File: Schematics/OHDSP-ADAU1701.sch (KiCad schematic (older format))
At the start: 0 parts

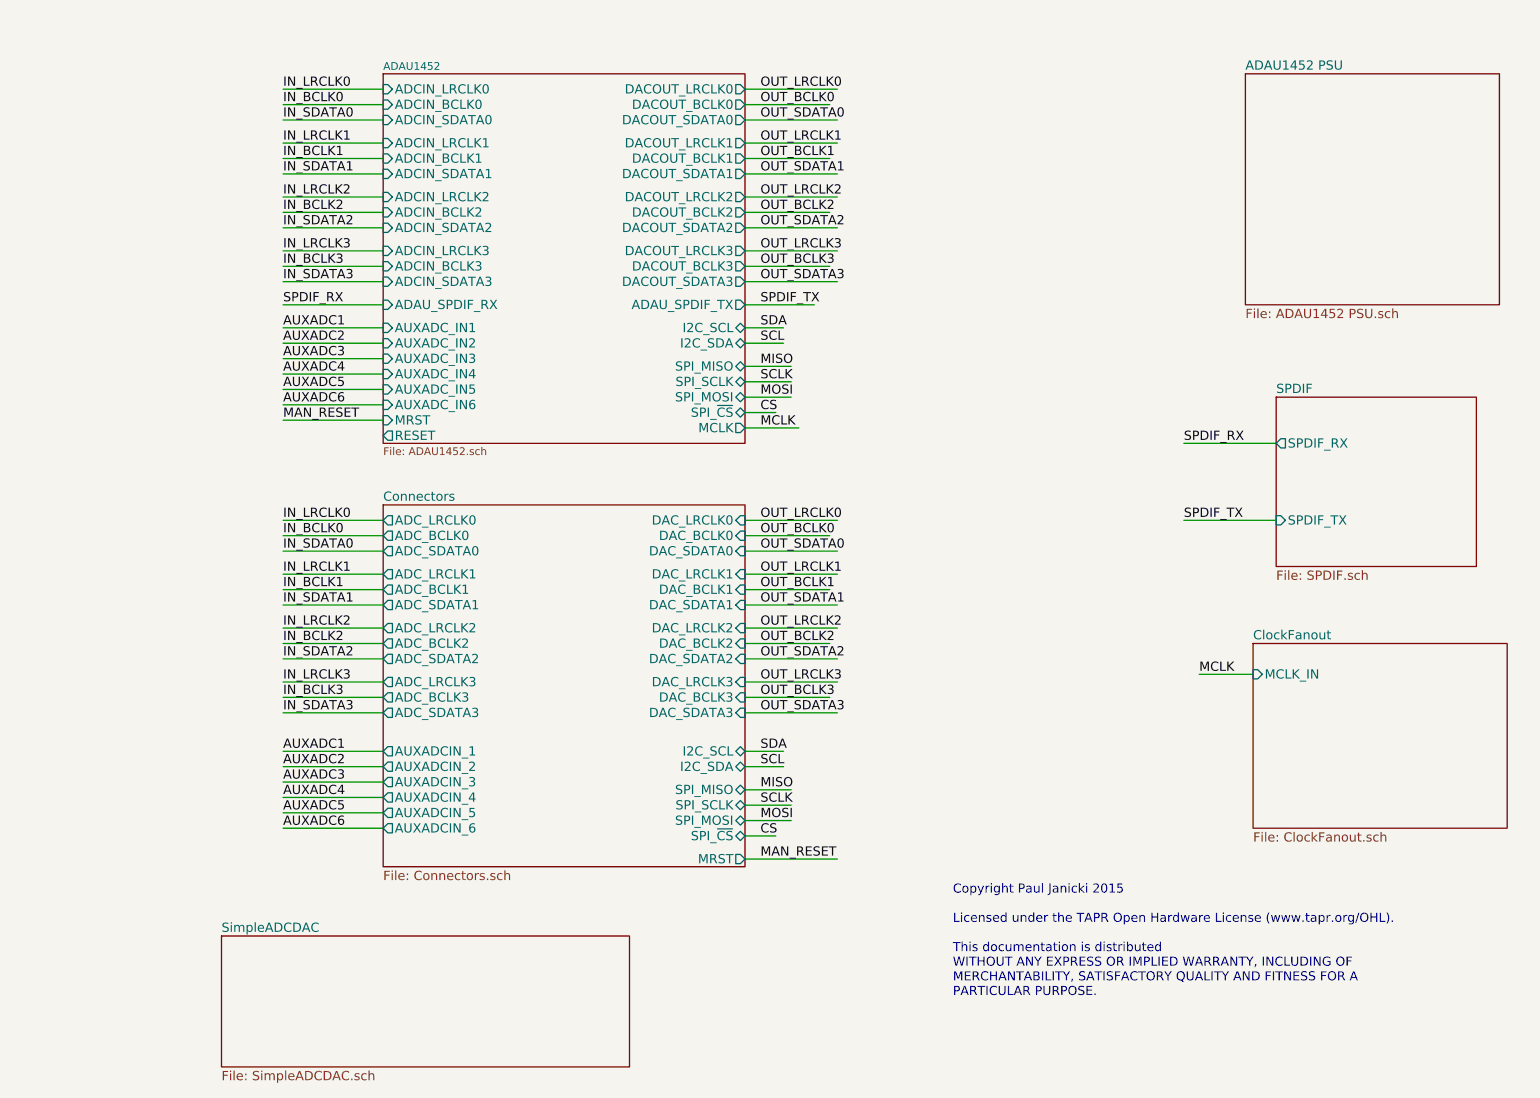
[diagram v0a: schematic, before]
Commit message: Adding ADAU1701 version
Because its easier...
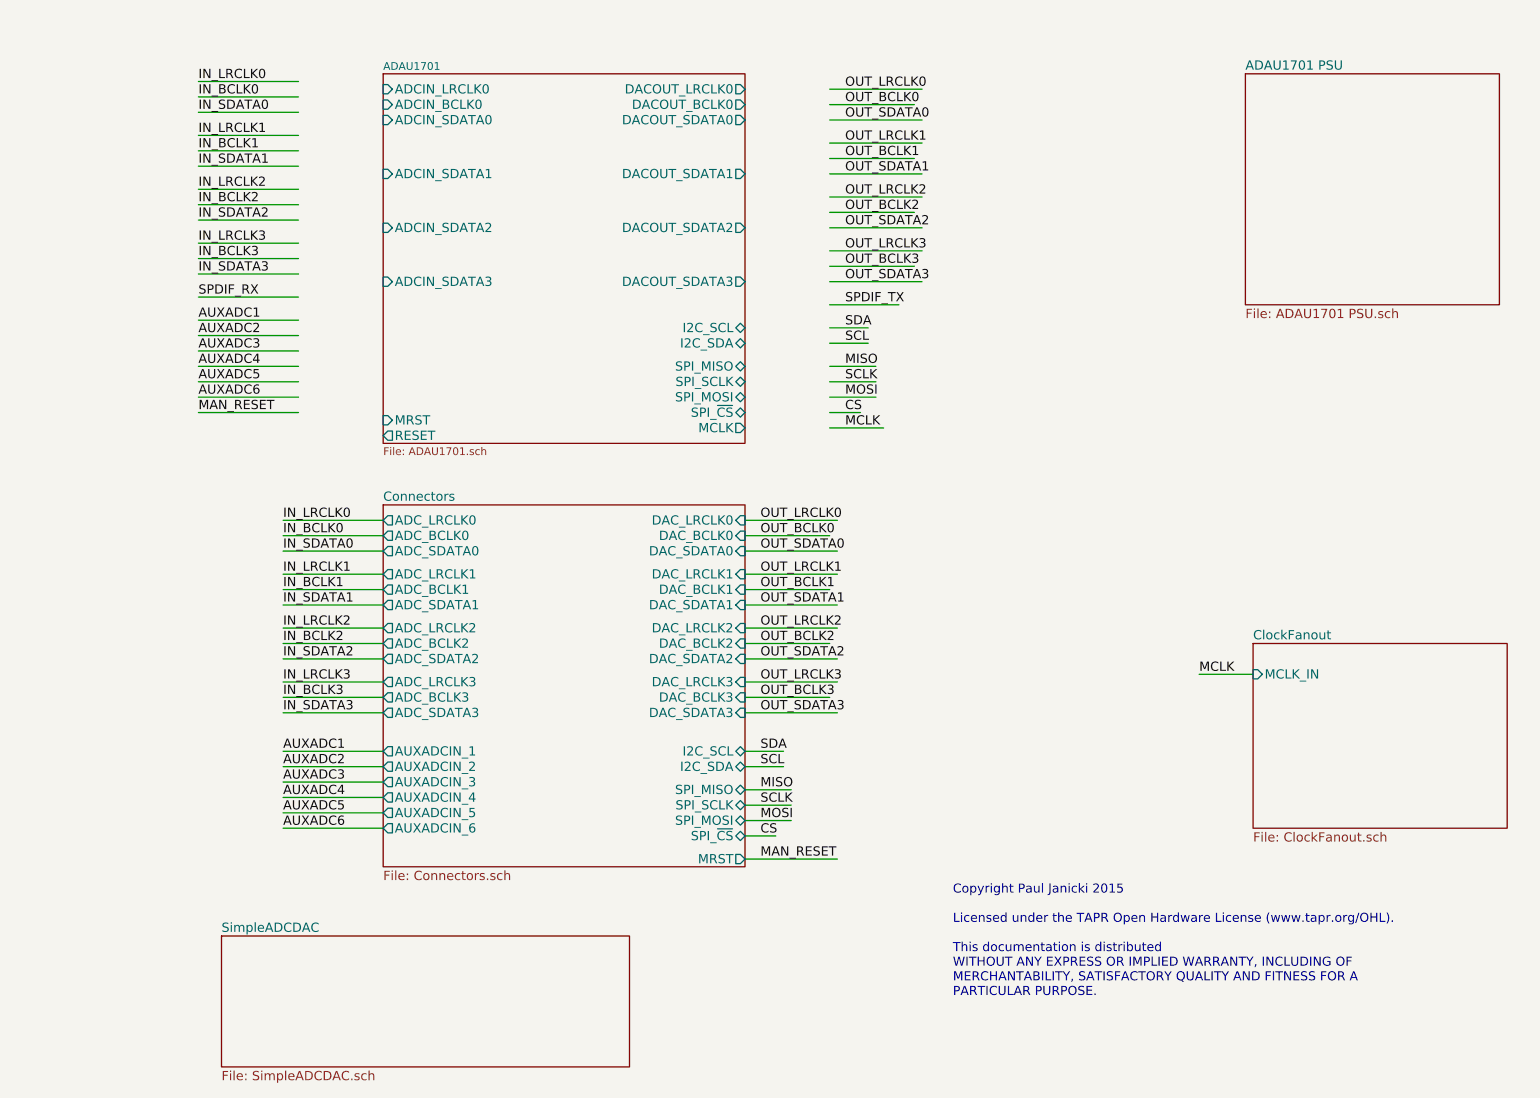
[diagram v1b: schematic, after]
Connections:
- wire segments 80 -> 78
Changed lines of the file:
@@
 LIBS:power
 LIBS:OHDSP-Lib
-LIBS:OHDSP-ADAU1452-cache
 EELAYER 25 0
 EELAYER END
 $Descr A4 11693 8268
 encoding utf-8
-Sheet 1 7
+Sheet 1 6
 Title ""
 Date "10 feb 2015"
@@
 S 3300 1100 2350 2400
 U 54BE4270
-F0 "ADAU1452" 50
-F1 "ADAU1452.sch" 50
+F0 "ADAU1701" 50
+F1 "ADAU1701.sch" 50
 F2 "ADCIN_LRCLK0" I L 3300 1200 60
 F3 "ADCIN_BCLK0" I L 3300 1300 60
 F4 "ADCIN_SDATA0" I L 3300 1400 60
-F5 "ADCIN_LRCLK1" I L 3300 1550 60
-F6 "ADCIN_BCLK1" I L 3300 1650 60
 F7 "ADCIN_SDATA1" I L 3300 1750 60
-F8 "ADCIN_LRCLK2" I L 3300 1900 60
-F9 "ADCIN_BCLK2" I L 3300 2000 60
 F10 "ADCIN_SDATA2" I L 3300 2100 60
-F11 "ADCIN_LRCLK3" I L 3300 2250 60
-F12 "ADCIN_BCLK3" I L 3300 2350 60
 F13 "ADCIN_SDATA3" I L 3300 2450 60
 F14 "DACOUT_LRCLK0" O R 5650 1200 60
 F15 "DACOUT_BCLK0" O R 5650 1300 60
 F16 "DACOUT_SDATA0" O R 5650 1400 60
-F17 "ADAU_SPDIF_RX" I L 3300 2600 60
-F18 "ADAU_SPDIF_TX" O R 5650 2600 60
-F19 "DACOUT_LRCLK1" O R 5650 1550 60
-F20 "DACOUT_BCLK1" O R 5650 1650 60
 F21 "DACOUT_SDATA1" O R 5650 1750 60
-F22 "DACOUT_LRCLK2" O R 5650 1900 60
-F23 "DACOUT_BCLK2" O R 5650 2000 60
 F24 "DACOUT_SDATA2" O R 5650 2100 60
-F25 "DACOUT_LRCLK3" O R 5650 2250 60
-F26 "DACOUT_BCLK3" O R 5650 2350 60
 F27 "DACOUT_SDATA3" O R 5650 2450 60
-F28 "AUXADC_IN1" I L 3300 2750 60
-F29 "AUXADC_IN2" I L 3300 2850 60
-F30 "AUXADC_IN3" I L 3300 2950 60
-F31 "AUXADC_IN4" I L 3300 3050 60
-F32 "AUXADC_IN5" I L 3300 3150 60
-F33 "AUXADC_IN6" I L 3300 3250 60
 F34 "I2C_SCL" B R 5650 2750 60
 F35 "I2C_SDA" B R 5650 2850 60
@@
 S 8900 1100 1650 1500
 U 54DA50D9
-F0 "ADAU1452 PSU" 60
-F1 "ADAU1452 PSU.sch" 60
+F0 "ADAU1701 PSU" 60
+F1 "ADAU1701 PSU.sch" 60
 $EndSheet
 $Sheet
@@
 F2 "MCLK_IN" I L 8950 5000 60
 $EndSheet
-$Sheet
-S 9100 3200 1300 1100
-U 54E30917
-F0 "SPDIF" 60
-F1 "SPDIF.sch" 60
-F2 "SPDIF_RX" O L 9100 3500 60
-F3 "SPDIF_TX" I L 9100 4000 60
-$EndSheet
-Text Label 2650 1200 0    60   ~ 0
+Text Label 2100 1150 0    60   ~ 0
 IN_LRCLK0
-Text Label 2650 1300 0    60   ~ 0
+Text Label 2100 1250 0    60   ~ 0
 IN_BCLK0
-Text Label 2650 1400 0    60   ~ 0
+Text Label 2100 1350 0    60   ~ 0
 IN_SDATA0
-Text Label 2650 1550 0    60   ~ 0
+Text Label 2100 1500 0    60   ~ 0
 IN_LRCLK1
-Text Label 2650 1650 0    60   ~ 0
+Text Label 2100 1600 0    60   ~ 0
 IN_BCLK1
-Text Label 2650 1750 0    60   ~ 0
+Text Label 2100 1700 0    60   ~ 0
 IN_SDATA1
-Text Label 2650 2450 0    60   ~ 0
+Text Label 2100 2400 0    60   ~ 0
 IN_SDATA3
-Text Label 2650 2350 0    60   ~ 0
+Text Label 2100 2300 0    60   ~ 0
 IN_BCLK3
-Text Label 2650 2250 0    60   ~ 0
+Text Label 2100 2200 0    60   ~ 0
 IN_LRCLK3
-Text Label 2650 2100 0    60   ~ 0
+Text Label 2100 2050 0    60   ~ 0
 IN_SDATA2
-Text Label 2650 2000 0    60   ~ 0
+Text Label 2100 1950 0    60   ~ 0
 IN_BCLK2
-Text Label 2650 1900 0    60   ~ 0
+Text Label 2100 1850 0    60   ~ 0
 IN_LRCLK2
 Wire Wire Line
-	2650 1200 3300 1200
-Wire Wire Line
-	3300 1300 2650 1300
-Wire Wire Line
-	2650 1400 3300 1400
-Wire Wire Line
-	3300 1550 2650 1550
-Wire Wire Line
-	2650 1650 3300 1650
-Wire Wire Line
-	3300 1750 2650 1750
-Wire Wire Line
-	3300 1900 2650 1900
-Wire Wire Line
-	2650 2000 3300 2000
-Wire Wire Line
-	3300 2100 2650 2100
-Wire Wire Line
-	2650 2250 3300 2250
-Wire Wire Line
-	3300 2350 2650 2350
-Wire Wire Line
-	2650 2450 3300 2450
-Text Label 5750 1200 0    60   ~ 0
+	2100 1150 2750 1150
+Wire Wire Line
+	2750 1250 2100 1250
+Wire Wire Line
+	2100 1350 2750 1350
+Wire Wire Line
+	2750 1500 2100 1500
+Wire Wire Line
+	2100 1600 2750 1600
+Wire Wire Line
+	2750 1700 2100 1700
+Wire Wire Line
+	2750 1850 2100 1850
+Wire Wire Line
+	2100 1950 2750 1950
+Wire Wire Line
+	2750 2050 2100 2050
+Wire Wire Line
+	2100 2200 2750 2200
+Wire Wire Line
+	2750 2300 2100 2300
+Wire Wire Line
+	2100 2400 2750 2400
+Text Label 6300 1200 0    60   ~ 0
 OUT_LRCLK0
-Text Label 5750 1300 0    60   ~ 0
+Text Label 6300 1300 0    60   ~ 0
 OUT_BCLK0
-Text Label 5750 1400 0    60   ~ 0
+Text Label 6300 1400 0    60   ~ 0
 OUT_SDATA0
 Wire Wire Line
-	5650 1200 6250 1200
-Wire Wire Line
-	6200 1300 5650 1300
-Wire Wire Line
-	5650 1400 6250 1400
-Text Label 5750 1550 0    60   ~ 0
+	6200 1200 6800 1200
+Wire Wire Line
+	6750 1300 6200 1300
+Wire Wire Line
+	6200 1400 6800 1400
+Text Label 6300 1550 0    60   ~ 0
 OUT_LRCLK1
-Text Label 5750 1650 0    60   ~ 0
+Text Label 6300 1650 0    60   ~ 0
 OUT_BCLK1
-Text Label 5750 1750 0    60   ~ 0
+Text Label 6300 1750 0    60   ~ 0
 OUT_SDATA1
 Wire Wire Line
-	5650 1550 6250 1550
-Wire Wire Line
-	6200 1650 5650 1650
-Wire Wire Line
-	5650 1750 6250 1750
-Text Label 5750 1900 0    60   ~ 0
+	6200 1550 6800 1550
+Wire Wire Line
+	6750 1650 6200 1650
+Wire Wire Line
+	6200 1750 6800 1750
+Text Label 6300 1900 0    60   ~ 0
 OUT_LRCLK2
-Text Label 5750 2000 0    60   ~ 0
+Text Label 6300 2000 0    60   ~ 0
 OUT_BCLK2
-Text Label 5750 2100 0    60   ~ 0
+Text Label 6300 2100 0    60   ~ 0
 OUT_SDATA2
 Wire Wire Line
-	5650 1900 6250 1900
-Wire Wire Line
-	6200 2000 5650 2000
-Wire Wire Line
-	5650 2100 6250 2100
-Text Label 5750 2250 0    60   ~ 0
+	6200 1900 6800 1900
+Wire Wire Line
+	6750 2000 6200 2000
+Wire Wire Line
+	6200 2100 6800 2100
+Text Label 6300 2250 0    60   ~ 0
 OUT_LRCLK3
-Text Label 5750 2350 0    60   ~ 0
+Text Label 6300 2350 0    60   ~ 0
 OUT_BCLK3
-Text Label 5750 2450 0    60   ~ 0
+Text Label 6300 2450 0    60   ~ 0
 OUT_SDATA3
 Wire Wire Line
-	5650 2250 6250 2250
-Wire Wire Line
-	6200 2350 5650 2350
-Wire Wire Line
-	5650 2450 6250 2450
+	6200 2250 6800 2250
+Wire Wire Line
+	6750 2350 6200 2350
+Wire Wire Line
+	6200 2450 6800 2450
 $Sheet
 S 3300 3900 2350 2350
@@
 Wire Wire Line
 	5650 5250 6250 5250
-Text Label 5750 2600 0    60   ~ 0
+Text Label 6300 2600 0    60   ~ 0
 SPDIF_TX
-Text Label 2650 2600 0    60   ~ 0
+Text Label 2100 2550 0    60   ~ 0
 SPDIF_RX
-Text Label 8500 3500 0    60   ~ 0
-SPDIF_RX
-Text Label 8500 4000 0    60   ~ 0
-SPDIF_TX
-Wire Wire Line
-	8500 4000 9100 4000
-Wire Wire Line
-	9100 3500 8500 3500
-Wire Wire Line
-	5650 2600 6100 2600
-Wire Wire Line
-	2650 2600 3300 2600
-Text Label 2650 3050 0    60   ~ 0
+Wire Wire Line
+	6200 2600 6650 2600
+Wire Wire Line
+	2100 2550 2750 2550
+Text Label 2100 3000 0    60   ~ 0
 AUXADC4
-Text Label 2650 3150 0    60   ~ 0
+Text Label 2100 3100 0    60   ~ 0
 AUXADC5
-Text Label 2650 3250 0    60   ~ 0
+Text Label 2100 3200 0    60   ~ 0
 AUXADC6
-Text Label 2650 2750 0    60   ~ 0
+Text Label 2100 2700 0    60   ~ 0
 AUXADC1
-Text Label 2650 2850 0    60   ~ 0
+Text Label 2100 2800 0    60   ~ 0
 AUXADC2
-Text Label 2650 2950 0    60   ~ 0
+Text Label 2100 2900 0    60   ~ 0
 AUXADC3
 Wire Wire Line
-	2650 2750 3300 2750
-Wire Wire Line
-	3300 2850 2650 2850
-Wire Wire Line
-	2650 2950 3300 2950
-Wire Wire Line
-	3300 3050 2650 3050
-Wire Wire Line
-	2650 3150 3300 3150
-Wire Wire Line
-	3300 3250 2650 3250
-Text Label 5750 3400 0    60   ~ 0
+	2100 2700 2750 2700
+Wire Wire Line
+	2750 2800 2100 2800
+Wire Wire Line
+	2100 2900 2750 2900
+Wire Wire Line
+	2750 3000 2100 3000
+Wire Wire Line
+	2100 3100 2750 3100
+Wire Wire Line
+	2750 3200 2100 3200
+Text Label 6300 3400 0    60   ~ 0
 MCLK
 Wire Wire Line
-	5650 3400 6000 3400
+	6200 3400 6550 3400
 Text Label 8600 5000 0    60   ~ 0
 MCLK
 Wire Wire Line
 	8600 5000 8950 5000
-Text Label 5750 2750 0    60   ~ 0
+Text Label 6300 2750 0    60   ~ 0
 SDA
-Text Label 5750 2850 0    60   ~ 0
+Text Label 6300 2850 0    60   ~ 0
 SCL
-Text Label 5750 3000 0    60   ~ 0
+Text Label 6300 3000 0    60   ~ 0
 MISO
-Text Label 5750 3100 0    60   ~ 0
+Text Label 6300 3100 0    60   ~ 0
 SCLK
-Text Label 5750 3200 0    60   ~ 0
+Text Label 6300 3200 0    60   ~ 0
 MOSI
-Text Label 5750 3300 0    60   ~ 0
+Text Label 6300 3300 0    60   ~ 0
 CS
 Wire Wire Line
-	5650 2750 5900 2750
-Wire Wire Line
-	5650 2850 5900 2850
-Wire Wire Line
-	5650 3000 5950 3000
-Wire Wire Line
-	5650 3100 5950 3100
-Wire Wire Line
-	5650 3200 5950 3200
-Wire Wire Line
-	5650 3300 5850 3300
+	6200 2750 6450 2750
+Wire Wire Line
+	6200 2850 6450 2850
+Wire Wire Line
+	6200 3000 6500 3000
+Wire Wire Line
+	6200 3100 6500 3100
+Wire Wire Line
+	6200 3200 6500 3200
+Wire Wire Line
+	6200 3300 6400 3300
 Text Label 5750 5500 0    60   ~ 0
 SDA
@@
 Wire Wire Line
 	5650 6200 6250 6200
-Text Label 2650 3350 0    60   ~ 0
+Text Label 2100 3300 0    60   ~ 0
 MAN_RESET
 Wire Wire Line
-	2650 3350 3300 3350
+	2100 3300 2750 3300
 $Sheet
 S 2250 6700 2650 850

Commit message: WIP
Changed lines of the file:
@@
 Wire Wire Line
 	2100 3300 2750 3300
-$Sheet
-S 2250 6700 2650 850
-U 55019779
-F0 "SimpleADCDAC" 60
-F1 "SimpleADCDAC.sch" 60
-$EndSheet
 $EndSCHEMATC

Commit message: WIP
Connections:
- net labels removed: AUXADC1, AUXADC2, AUXADC3, AUXADC4, AUXADC5, AUXADC6, CS, IN_BCLK1, IN_BCLK2, IN_BCLK3, IN_LRCLK1, IN_LRCLK2, IN_LRCLK3, MISO, MOSI, OUT_BCLK1, OUT_BCLK2, OUT_BCLK3, OUT_LRCLK1, OUT_LRCLK2, OUT_LRCLK3, SCLK, SPDIF_RX, SPDIF_TX
- wire segments 78 -> 31
